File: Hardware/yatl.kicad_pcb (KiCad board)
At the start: 4 copper layers, 56.6 x 25.4 mm, 19 parts, among them J1 Conn_01x08_Male, J2 Conn_01x08_Male, SW1 SW_SPST, U2 ATmega328-A

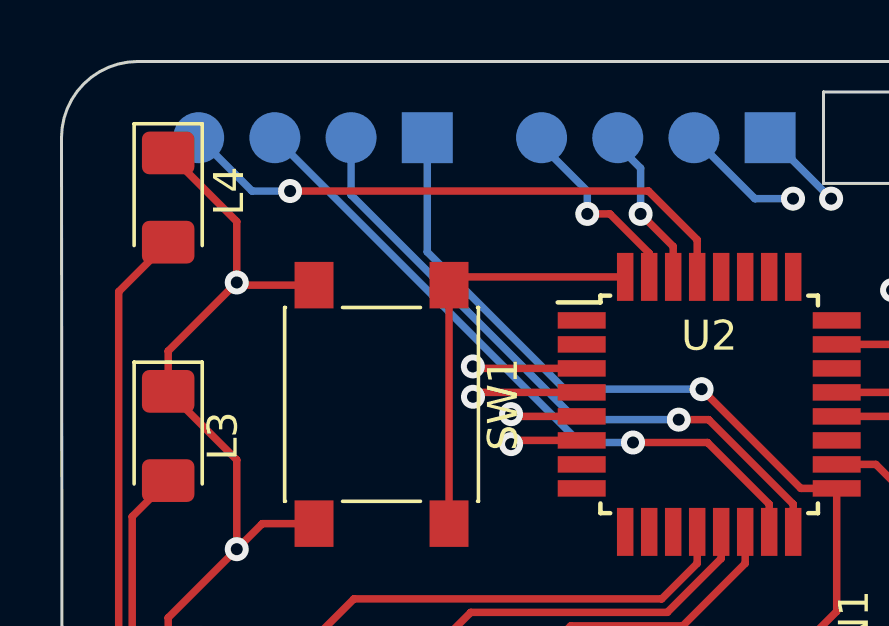
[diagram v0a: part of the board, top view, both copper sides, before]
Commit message: Fix pitch between connectors
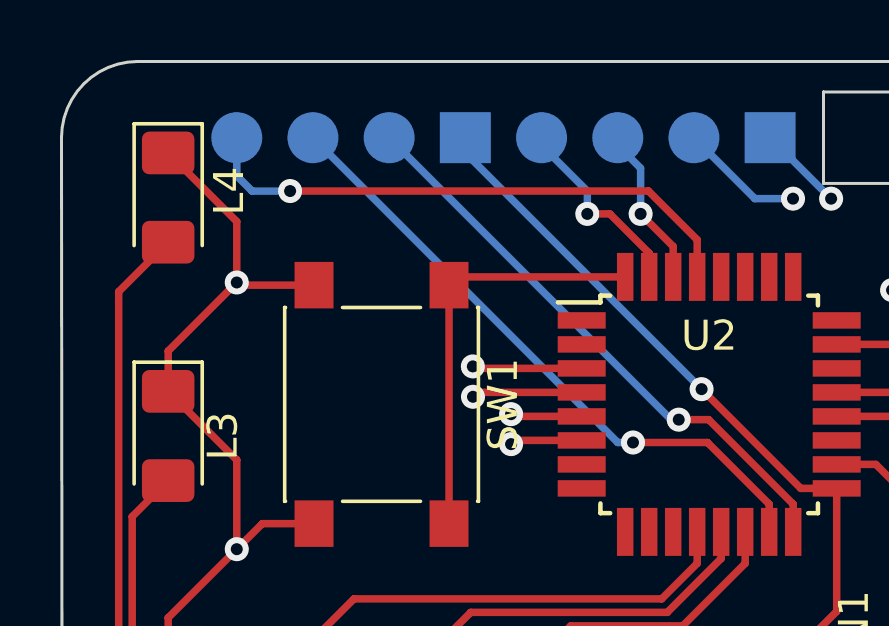
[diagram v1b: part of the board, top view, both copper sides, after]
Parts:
- moved J1 1.27 mm to (183.9, 94.0)
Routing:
- net /SCK: track 26.9 -> 23.7 mm
- net /MISO: track 21.8 -> 19.5 mm
- net /MOSI: track 22.5 -> 21.2 mm
- net /RESET: track 19.3 -> 18.7 mm
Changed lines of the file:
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@@
   )
   (footprint "yatl_library:Testpoint_1x04_P2.54mm" (layer "B.Cu")
-    (at 182.626 93.98 90)
+    (at 183.896 93.98 90)
     (descr "Through hole straight pin header, 1x04, 2.54mm pitch, single row")
     (tags "Through hole pin header THT 1x04 2.54mm single row")
@@
   (segment (start 190.000614 95.758) (end 178.054 95.758) (width 0.25) (layer "F.Cu") (net 4))
   (via (at 178.054 95.758) (size 0.8) (drill 0.4) (layers "F.Cu" "B.Cu") (net 4))
-  (segment (start 176.784 95.758) (end 175.006 93.98) (width 0.25) (layer "B.Cu") (net 4))
   (segment (start 178.054 95.758) (end 176.784 95.758) (width 0.25) (layer "B.Cu") (net 4))
+  (segment (start 176.276 95.25) (end 176.276 93.98) (width 0.25) (layer "B.Cu") (net 4))
+  (segment (start 176.784 95.758) (end 176.276 95.25) (width 0.25) (layer "B.Cu") (net 4))
   (segment (start 194.024 107.12) (end 194.024 106.195978) (width 0.25) (layer "F.Cu") (net 5))
   (segment (start 191.968022 104.14) (end 189.484 104.14) (width 0.25) (layer "F.Cu") (net 5))
   (segment (start 194.024 106.195978) (end 191.968022 104.14) (width 0.25) (layer "F.Cu") (net 5))
   (via (at 189.484 104.14) (size 0.8) (drill 0.4) (layers "F.Cu" "B.Cu") (net 5))
-  (segment (start 189.484 104.14) (end 187.706 104.14) (width 0.25) (layer "B.Cu") (net 5))
-  (segment (start 187.706 104.14) (end 177.546 93.98) (width 0.25) (layer "B.Cu") (net 5))
+  (segment (start 189.484 104.14) (end 188.976 104.14) (width 0.25) (layer "B.Cu") (net 5))
+  (segment (start 188.976 104.14) (end 178.816 93.98) (width 0.25) (layer "B.Cu") (net 5))
   (segment (start 194.824 106.195978) (end 192.006022 103.378) (width 0.25) (layer "F.Cu") (net 6))
   (segment (start 194.824 107.12) (end 194.824 106.195978) (width 0.25) (layer "F.Cu") (net 6))
   (segment (start 192.006022 103.378) (end 191.008 103.378) (width 0.25) (layer "F.Cu") (net 6))
   (via (at 191.008 103.378) (size 0.8) (drill 0.4) (layers "F.Cu" "B.Cu") (net 6))
-  (segment (start 191.008 103.378) (end 187.579718 103.378) (width 0.25) (layer "B.Cu") (net 6))
-  (segment (start 180.086 95.884282) (end 180.086 93.98) (width 0.25) (layer "B.Cu") (net 6))
-  (segment (start 187.579718 103.378) (end 180.086 95.884282) (width 0.25) (layer "B.Cu") (net 6))
+  (segment (start 191.008 103.378) (end 190.754 103.378) (width 0.25) (layer "B.Cu") (net 6))
+  (segment (start 190.754 103.378) (end 181.356 93.98) (width 0.25) (layer "B.Cu") (net 6))
   (segment (start 196.274 109.77) (end 194.818 111.226) (width 0.25) (layer "F.Cu") (net 7))
   (segment (start 195.078 105.67) (end 191.77 102.362) (width 0.25) (layer "F.Cu") (net 7))
@@
   (segment (start 196.274 105.67) (end 195.078 105.67) (width 0.25) (layer "F.Cu") (net 7))
   (via (at 191.77 102.362) (size 0.8) (drill 0.4) (layers "F.Cu" "B.Cu") (net 7))
-  (segment (start 182.626 97.788564) (end 182.626 93.98) (width 0.25) (layer "B.Cu") (net 7))
-  (segment (start 187.199436 102.362) (end 182.626 97.788564) (width 0.25) (layer "B.Cu") (net 7))
-  (segment (start 191.77 102.362) (end 187.199436 102.362) (width 0.25) (layer "B.Cu") (net 7))
+  (segment (start 183.896 93.98) (end 183.896 94.488) (width 0.25) (layer "B.Cu") (net 7))
+  (segment (start 183.896 94.488) (end 191.77 102.362) (width 0.25) (layer "B.Cu") (net 7))
   (segment (start 190.824 97.606) (end 189.738 96.52) (width 0.25) (layer "F.Cu") (net 8))
   (segment (start 190.824 98.62) (end 190.824 97.606) (width 0.25) (layer "F.Cu") (net 8))

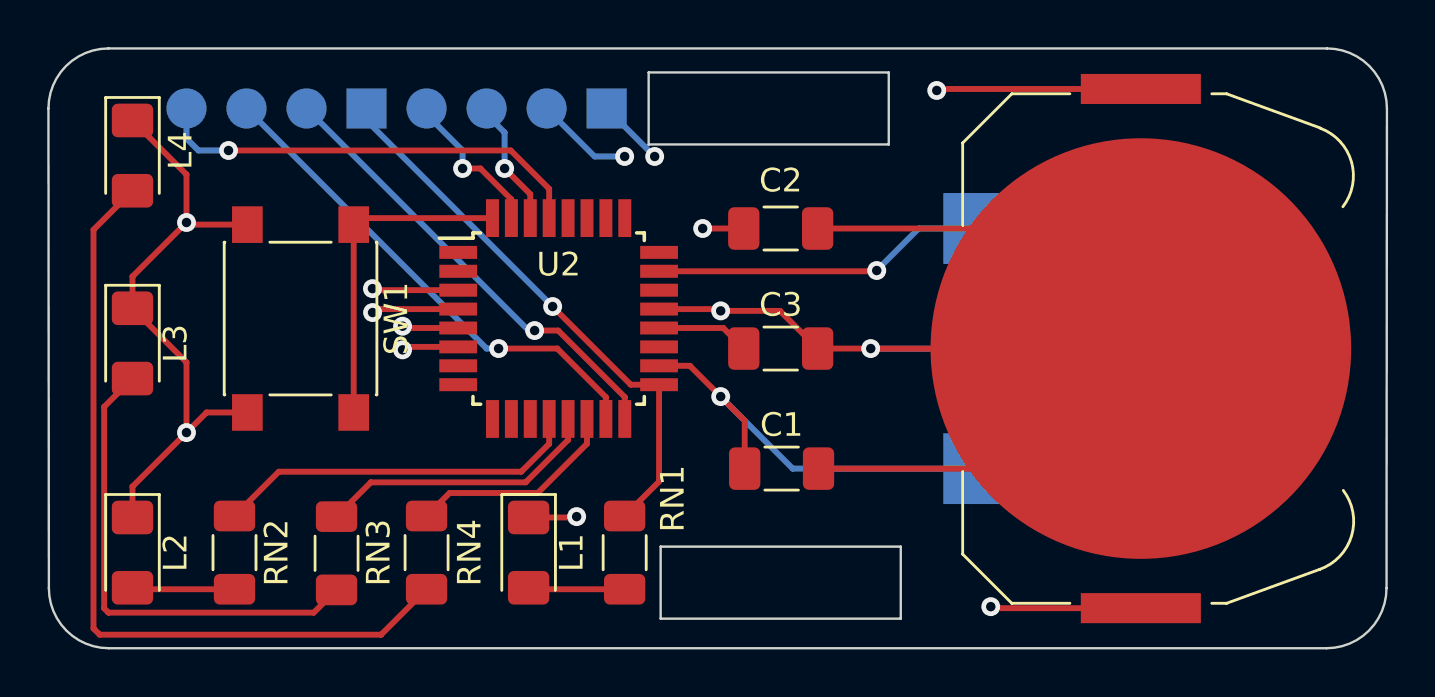
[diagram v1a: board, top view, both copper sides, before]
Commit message: Rename LED and reposition connector label
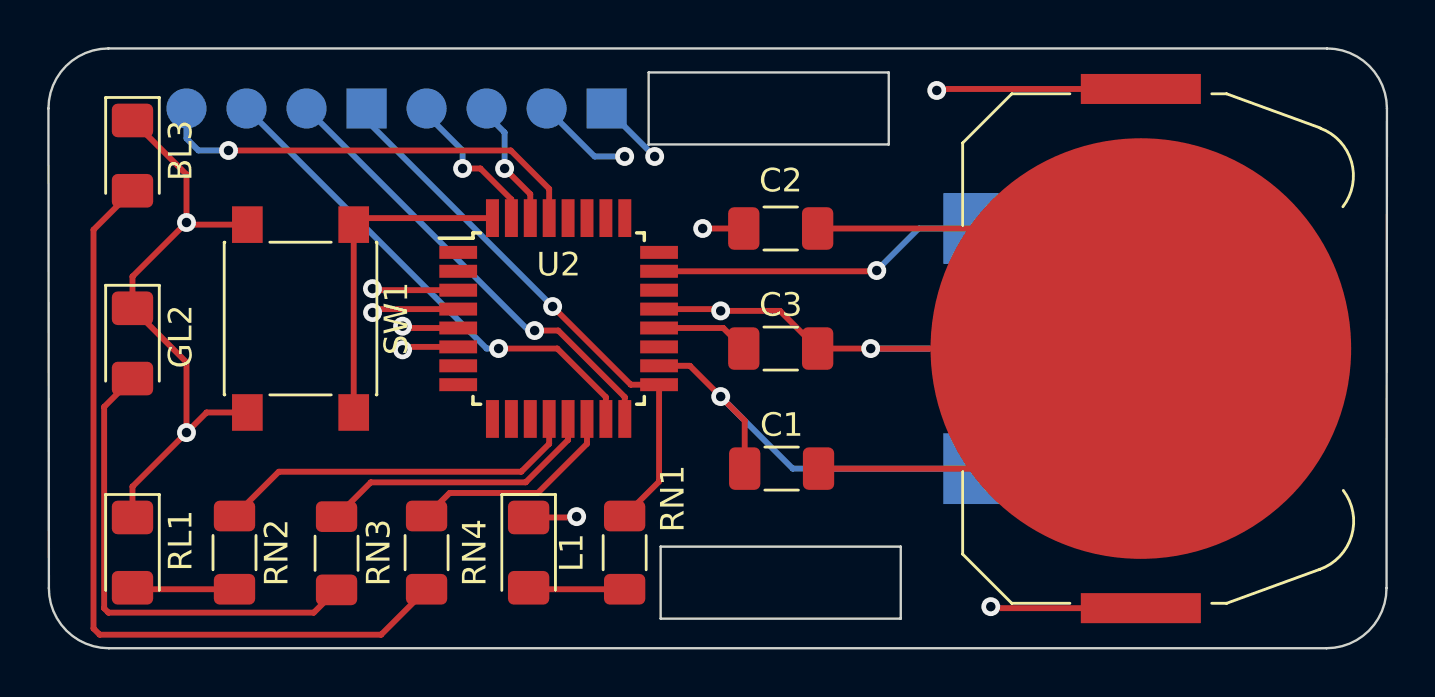
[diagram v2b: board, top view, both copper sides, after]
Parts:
- L2: value RED -> RL1
- L3: value GREEN -> GL2
- L4: value BLUE -> BL3
- RN1, RN2, RN3, RN4: value 100 -> 2k
- turned RN4 to 90 degrees
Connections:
- RN4 pad 1: /LED2 -> Net-(L4-Pad2)
- RN4 pad 2: Net-(L4-Pad2) -> /LED2
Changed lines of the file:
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@@
       (effects (font (size 1 1) (thickness 0.15)))
     )
-    (fp_text value "100" (at 0 1.82 90) (layer "F.Fab")
+    (fp_text value "2k" (at 0 1.82 90) (layer "F.Fab")
       (effects (font (size 1 1) (thickness 0.15)))
     )
@@
     (property "Sheetname" "")
     (attr smd)
-    (fp_text reference "L2" (at 0 -1.82 90) (layer "F.SilkS")
-      (effects (font (size 1 1) (thickness 0.15)))
-    )
-    (fp_text value "RED" (at 0 1.82 90) (layer "F.Fab")
+    (fp_text reference "L2" (at 0 -1.82 90) (layer "User.1")
+      (effects (font (size 1 1) (thickness 0.15)))
+    )
+    (fp_text value "RL1" (at -0.508 -2.032 90) (layer "F.SilkS")
       (effects (font (size 1 1) (thickness 0.15)))
     )
@@
       (effects (font (size 1 1) (thickness 0.15)))
     )
-    (fp_text value "100" (at 0 1.82 90) (layer "F.Fab")
+    (fp_text value "2k" (at 0 1.82 90) (layer "F.Fab")
       (effects (font (size 1 1) (thickness 0.15)))
     )
@@
   )
   (footprint "Resistor_SMD:R_1206_3216Metric_Pad1.30x1.75mm_HandSolder" (layer "F.Cu")
-    (at 186.436 112.776 -90)
+    (at 186.436 112.776 90)
     (descr "Resistor SMD 1206 (3216 Metric), square (rectangular) end terminal, IPC_7351 nominal with elongated pad for handsoldering. (Body size source: IPC-SM-782 page 72, https://www.pcb-3d.com/wordpress/wp-content/uploads/ipc-sm-782a_amendment_1_and_2.pdf), generated with kicad-footprint-generator")
     (tags "resistor handsolder")
@@
     (property "Sheetname" "")
     (attr smd)
-    (fp_text reference "RN4" (at 0 -1.82 90) (layer "F.SilkS")
-      (effects (font (size 1 1) (thickness 0.15)))
-    )
-    (fp_text value "100" (at 0 1.82 90) (layer "F.Fab")
+    (fp_text reference "RN4" (at 0 2.032 90) (layer "F.SilkS")
+      (effects (font (size 1 1) (thickness 0.15)))
+    )
+    (fp_text value "2k" (at 0 1.82 90) (layer "F.Fab")
       (effects (font (size 1 1) (thickness 0.15)))
     )
@@
     (fp_line (start 1.6 0.8) (end -1.6 0.8) (layer "F.Fab") (width 0.1))
     (fp_line (start -1.6 0.8) (end -1.6 -0.8) (layer "F.Fab") (width 0.1))
-    (pad "1" smd roundrect (at -1.55 0 270) (size 1.3 1.75) (layers "F.Cu" "F.Paste" "F.Mask") (roundrect_rratio 0.1923076923)
+    (pad "1" smd roundrect (at -1.55 0 90) (size 1.3 1.75) (layers "F.Cu" "F.Paste" "F.Mask") (roundrect_rratio 0.1923076923)
+      (net 32 "Net-(L4-Pad2)") (pintype "passive"))
+    (pad "2" smd roundrect (at 1.55 0 90) (size 1.3 1.75) (layers "F.Cu" "F.Paste" "F.Mask") (roundrect_rratio 0.1923076923)
       (net 15 "/LED2") (pintype "passive"))
-    (pad "2" smd roundrect (at 1.55 0 270) (size 1.3 1.75) (layers "F.Cu" "F.Paste" "F.Mask") (roundrect_rratio 0.1923076923)
-      (net 32 "Net-(L4-Pad2)") (pintype "passive"))
     (model "${KICAD6_3DMODEL_DIR}/Resistor_SMD.3dshapes/R_1206_3216Metric.wrl"
       (offset (xyz 0 0 0))
@@
     (property "Sheetname" "")
     (attr smd)
-    (fp_text reference "L3" (at 0 -1.82 90) (layer "F.SilkS")
-      (effects (font (size 1 1) (thickness 0.15)))
-    )
-    (fp_text value "GREEN" (at 0 1.82 90) (layer "F.Fab")
+    (fp_text reference "L3" (at 0 -1.82 90) (layer "User.1")
+      (effects (font (size 1 1) (thickness 0.15)))
+    )
+    (fp_text value "GL2" (at -0.2905 -2.032 90) (layer "F.SilkS")
       (effects (font (size 1 1) (thickness 0.15)))
     )
@@
     (property "Sheetname" "")
     (attr smd)
-    (fp_text reference "L4" (at -0.2175 -2.032 90) (layer "F.SilkS")
-      (effects (font (size 1 1) (thickness 0.15)))
-    )
-    (fp_text value "BLUE" (at 0 1.82 90) (layer "F.Fab")
+    (fp_text reference "L4" (at -0.2175 -2.032 90) (layer "User.1")
+      (effects (font (size 1 1) (thickness 0.15)))
+    )
+    (fp_text value "BL3" (at -0.2175 -2.032 90) (layer "F.SilkS")
       (effects (font (size 1 1) (thickness 0.15)))
     )
@@
       (effects (font (size 1 1) (thickness 0.15)))
     )
-    (fp_text value "100" (at 0 1.82 90) (layer "F.Fab")
+    (fp_text value "2k" (at 0 1.82 90) (layer "F.Fab")
       (effects (font (size 1 1) (thickness 0.15)))
     )
@@
   (gr_line (start 170.452051 114.281949) (end 170.434 93.98) (layer "Edge.Cuts") (width 0.1))
   (gr_rect (start 170.434 91.44) (end 227.076 116.84) (layer "User.1") (width 0.15) (fill none))
-  (gr_text "MOSI" (at 177.546 97.282 90) (layer "B.SilkS")
+  (gr_text "MOSI" (at 178.816 97.536 90) (layer "B.SilkS")
     (effects (font (size 1 1) (thickness 0.15)) (justify mirror))
   )
@@
     (effects (font (size 1 1) (thickness 0.15)) (justify mirror))
   )
-  (gr_text "SCK" (at 182.626 97.028 90) (layer "B.SilkS")
+  (gr_text "SCK" (at 183.896 97.282 90) (layer "B.SilkS")
     (effects (font (size 1 1) (thickness 0.15)) (justify mirror))
   )
@@
     (effects (font (size 1 1) (thickness 0.15)) (justify mirror))
   )
-  (gr_text "MISO" (at 180.086 97.282 90) (layer "B.SilkS")
+  (gr_text "MISO" (at 181.356 97.536 90) (layer "B.SilkS")
     (effects (font (size 1 1) (thickness 0.15)) (justify mirror))
   )
@@
     (effects (font (size 1 1) (thickness 0.15)) (justify mirror))
   )
-  (gr_text "RST" (at 175.006 96.774 90) (layer "B.SilkS")
+  (gr_text "RST" (at 176.276 97.028 90) (layer "B.SilkS")
     (effects (font (size 1 1) (thickness 0.15)) (justify mirror))
   )
@@
   (segment (start 192.424 107.12) (end 192.424 108.005717) (width 0.25) (layer "F.Cu") (net 14))
   (segment (start 193.224 108.17) (end 191.14252 110.25148) (width 0.25) (layer "F.Cu") (net 15))
+  (segment (start 193.224 107.12) (end 193.224 108.17) (width 0.25) (layer "F.Cu") (net 15))
   (segment (start 187.41052 110.25148) (end 186.436 111.226) (width 0.25) (layer "F.Cu") (net 15))
-  (segment (start 193.224 107.12) (end 193.224 108.17) (width 0.25) (layer "F.Cu") (net 15))
   (segment (start 191.14252 110.25148) (end 187.41052 110.25148) (width 0.25) (layer "F.Cu") (net 15))
   (segment (start 189.224 98.62) (end 183.627 98.62) (width 0.25) (layer "F.Cu") (net 16))
@@
   (segment (start 207.264 99.06) (end 209.804 99.06) (width 0.25) (layer "B.Cu") (net 17))
   (segment (start 205.486 100.838) (end 207.264 99.06) (width 0.25) (layer "B.Cu") (net 17))
-  (segment (start 186.436 114.326) (end 184.512789 116.249211) (width 0.25) (layer "F.Cu") (net 32))
   (segment (start 172.34096 99.11204) (end 173.99 97.463) (width 0.25) (layer "F.Cu") (net 32))
   (segment (start 172.604193 116.249211) (end 172.34096 115.985978) (width 0.25) (layer "F.Cu") (net 32))
   (segment (start 172.34096 115.985978) (end 172.34096 99.11204) (width 0.25) (layer "F.Cu") (net 32))
   (segment (start 184.512789 116.249211) (end 172.604193 116.249211) (width 0.25) (layer "F.Cu") (net 32))
+  (segment (start 184.512789 116.249211) (end 186.436 114.326) (width 0.25) (layer "F.Cu") (net 32))
   (zone (net 2) (net_name "GND") (layer "In1.Cu") (hatch edge 0.508)
     (connect_pads (clearance 0.508))

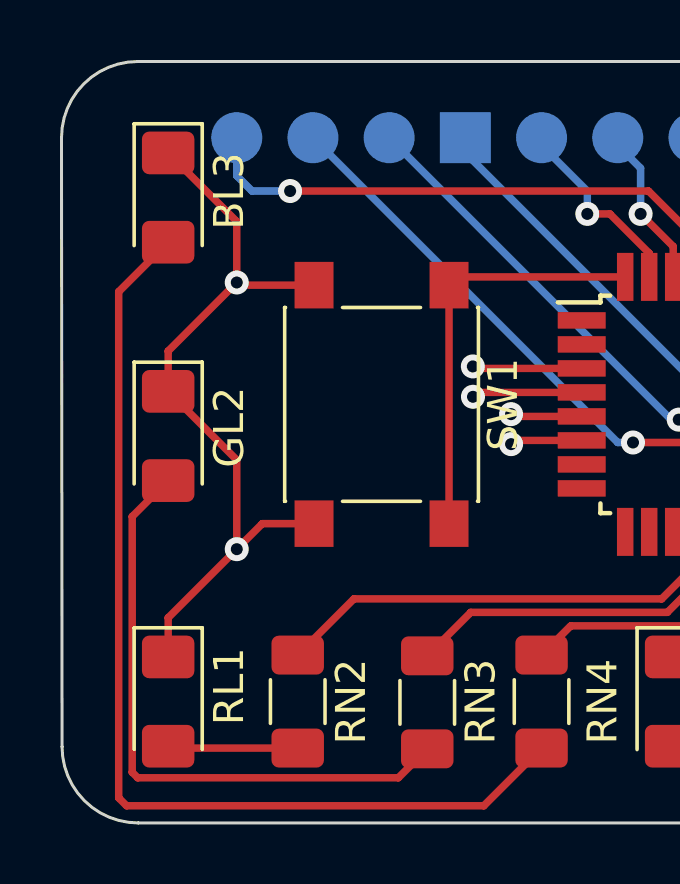
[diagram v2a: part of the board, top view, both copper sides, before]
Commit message: Increase LED resistor value to reduce current consumption
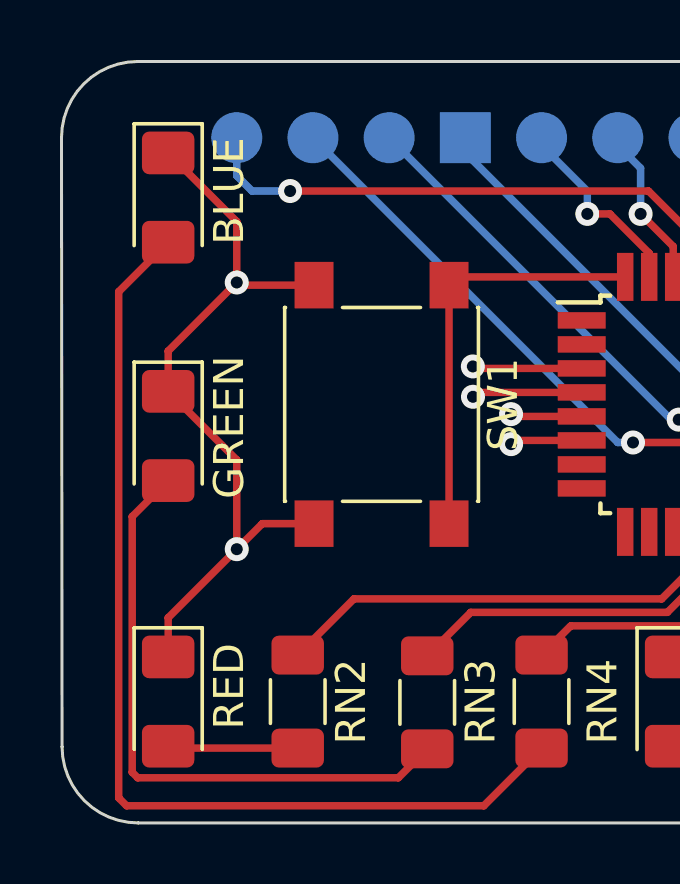
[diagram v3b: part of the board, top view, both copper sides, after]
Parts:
- L2: value RL1 -> RED
- L3: value GL2 -> GREEN
- L4: value BL3 -> BLUE
- RN1, RN2, RN3, RN4: value 2k -> 3k3
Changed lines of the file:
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@@
       (effects (font (size 1 1) (thickness 0.15)))
     )
-    (fp_text value "2k" (at 0 1.82 90) (layer "F.Fab")
+    (fp_text value "3k3" (at 0 1.82 90) (layer "F.Fab")
       (effects (font (size 1 1) (thickness 0.15)))
     )
@@
       (effects (font (size 1 1) (thickness 0.15)))
     )
-    (fp_text value "RL1" (at -0.508 -2.032 90) (layer "F.SilkS")
+    (fp_text value "RED" (at -0.508 -2.032 90) (layer "F.SilkS")
       (effects (font (size 1 1) (thickness 0.15)))
     )
@@
       (effects (font (size 1 1) (thickness 0.15)))
     )
-    (fp_text value "2k" (at 0 1.82 90) (layer "F.Fab")
+    (fp_text value "3k3" (at 0 1.82 90) (layer "F.Fab")
       (effects (font (size 1 1) (thickness 0.15)))
     )
@@
       (effects (font (size 1 1) (thickness 0.15)))
     )
-    (fp_text value "2k" (at 0 1.82 90) (layer "F.Fab")
+    (fp_text value "3k3" (at 0 1.82 90) (layer "F.Fab")
       (effects (font (size 1 1) (thickness 0.15)))
     )
@@
       (effects (font (size 1 1) (thickness 0.15)))
     )
-    (fp_text value "GL2" (at -0.2905 -2.032 90) (layer "F.SilkS")
+    (fp_text value "GREEN" (at -0.2905 -2.032 90) (layer "F.SilkS")
       (effects (font (size 1 1) (thickness 0.15)))
     )
@@
       (effects (font (size 1 1) (thickness 0.15)))
     )
-    (fp_text value "BL3" (at -0.2175 -2.032 90) (layer "F.SilkS")
+    (fp_text value "BLUE" (at -0.2175 -2.032 90) (layer "F.SilkS")
       (effects (font (size 1 1) (thickness 0.15)))
     )
@@
       (effects (font (size 1 1) (thickness 0.15)))
     )
-    (fp_text value "2k" (at 0 1.82 90) (layer "F.Fab")
-      (effects (font (size 1 1) (thickness 0.15)))
-    )
+    (fp_text value "3k3" (at 0 1.82 90) (layer "F.Fab")
+      (effects (font (size 1 1) (thickness 0.15)))
+    )
